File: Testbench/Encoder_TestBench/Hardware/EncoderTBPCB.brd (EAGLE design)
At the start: 51.7 x 81.3 mm, 17 parts, among them IC1 7805DT, U1 ATMEGA328P-PU, X1 C-GRID-05-15-91

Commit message: Upload upon Design Review
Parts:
- removed R3: 1MΩ, resistor:R0603
- C1: value 100nF -> 0.1µF
- C2, C3: value 100nF -> 10µF
- R1: value 220Ω -> 220
- R2: value 200Ω -> 200
- R4: value 850Ω -> 850
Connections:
- net N$10: no longer R3.2
- net N$11: no longer R3.1
- net N$13: now also U1.4; no longer U1.3
- net N$14: now also U1.5; no longer U1.4
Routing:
- net N$14: track 26.9 -> 29.4 mm
- net N$13: track 28.9 -> 31.4 mm
- net N$10: track 39.7 -> 37.8 mm
- net N$11: track 41.4 -> 39.7 mm
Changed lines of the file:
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@@
 </autorouter>
 <elements>
-<element name="C1" library="resistor" package="C0603" value="100nF" x="69.85" y="40.64" rot="R270"/>
-<element name="C2" library="resistor" package="C0603" value="100nF" x="80.01" y="63.5"/>
-<element name="C3" library="resistor" package="C0603" value="100nF" x="83.82" y="63.5"/>
+<element name="C1" library="resistor" package="C0603" value="0.1µF" x="69.85" y="40.64" rot="R270"/>
+<element name="C2" library="resistor" package="C0603" value="10µF" x="80.01" y="63.5"/>
+<element name="C3" library="resistor" package="C0603" value="10µF" x="83.82" y="63.5"/>
 <element name="C4" library="resistor" package="C0603" value="22pF" x="77.47" y="16.51" rot="R180"/>
 <element name="C5" library="resistor" package="C0603" value="22pF" x="85.09" y="16.51"/>
@@
 <element name="JP1" library="pinhead" package="2X03" value="" x="57.15" y="31.75" rot="R90"/>
 <element name="Q1" library="special" package="QS" value="" x="81.28" y="8.89" rot="R180"/>
-<element name="R1" library="resistor" package="R0603" value="220Ω" x="90.17" y="38.1"/>
-<element name="R3" library="resistor" package="R0603" value="1MΩ" x="81.28" y="16.51" rot="R180"/>
-<element name="R4" library="resistor" package="R0603" value="850Ω" x="90.17" y="67.31" rot="R90"/>
+<element name="R1" library="resistor" package="R0603" value="220" x="90.17" y="38.1"/>
+<element name="R4" library="resistor" package="R0603" value="850" x="90.17" y="67.31" rot="R90"/>
 <element name="U1" library="Atmel_By_element14_Batch_1-00" package="DIP254P762X457-28" value="ATMEGA328P-PU" x="74.93" y="57.15" rot="R180">
 <attribute name="OC_FARNELL" value="1715487" x="74.93" y="57.15" size="1.778" layer="27" rot="R180" display="off"/>
@@
 <attribute name="SUPPLIER" value="Atmel" x="74.93" y="57.15" size="1.778" layer="27" rot="R180" display="off"/>
 </element>
-<element name="R2" library="resistor" package="R0603" value="200Ω" x="90.17" y="33.02"/>
+<element name="R2" library="resistor" package="R0603" value="200" x="90.17" y="33.02"/>
 <element name="X1" library="con-molex" package="15-91-05" value="C-GRID-05-15-91" x="53.34" y="13.97" rot="R90"/>
 <element name="JP2" library="pinhead" package="1X16" value="" x="96.52" y="52.07" rot="R270"/>
@@
 </signal>
 <signal name="N$13">
-<contactref element="U1" pad="3"/>
 <contactref element="X1" pad="1"/>
 <wire x1="65.7225" y1="8.89" x2="80.01" y2="23.1775" width="0.254" layer="1"/>
 <wire x1="64.135" y1="8.89" x2="65.7225" y2="8.89" width="0.254" layer="1"/>
-<wire x1="82.55" y1="29.21" x2="80.01" y2="26.67" width="0.254" layer="1"/>
-<wire x1="80.01" y1="26.67" x2="80.01" y2="23.1775" width="0.254" layer="1"/>
+<wire x1="80.01" y1="29.21" x2="80.01" y2="23.1775" width="0.254" layer="1"/>
+<contactref element="U1" pad="4"/>
+<wire x1="80.01" y1="29.21" x2="82.55" y2="31.75" width="0.254" layer="1"/>
 </signal>
 <signal name="N$14">
-<contactref element="U1" pad="4"/>
 <contactref element="X1" pad="3"/>
 <wire x1="66.675" y1="13.97" x2="78.74" y2="26.035" width="0.254" layer="1"/>
 <wire x1="64.135" y1="13.97" x2="66.675" y2="13.97" width="0.254" layer="1"/>
-<wire x1="82.55" y1="31.75" x2="78.74" y2="27.94" width="0.254" layer="1"/>
-<wire x1="78.74" y1="27.94" x2="78.74" y2="26.035" width="0.254" layer="1"/>
+<contactref element="U1" pad="5"/>
+<wire x1="78.74" y1="30.48" x2="82.55" y2="34.29" width="0.254" layer="1"/>
+<wire x1="78.74" y1="26.035" x2="78.74" y2="30.48" width="0.254" layer="1"/>
 </signal>
 <signal name="N$15">
@@
 <contactref element="Q1" pad="2"/>
 <contactref element="C4" pad="1"/>
-<contactref element="R3" pad="2"/>
 <contactref element="U1" pad="9"/>
-<wire x1="80.43" y1="16.51" x2="78.74" y2="16.51" width="0.254" layer="1"/>
 <wire x1="78.74" y1="8.89" x2="78.74" y2="16.51" width="0.254" layer="1"/>
 <wire x1="78.74" y1="16.51" x2="78.32" y2="16.51" width="0.254" layer="1"/>
@@
 <wire x1="80.645" y1="17.145" x2="83.82" y2="20.32" width="0.254" layer="1"/>
 <wire x1="80.645" y1="16.51" x2="80.645" y2="17.145" width="0.254" layer="1"/>
-<wire x1="80.645" y1="16.51" x2="80.43" y2="16.51" width="0.254" layer="1"/>
+<wire x1="78.74" y1="16.51" x2="80.645" y2="16.51" width="0" layer="19" extent="1-1"/>
 </signal>
 <signal name="N$11">
 <contactref element="Q1" pad="1"/>
 <contactref element="C5" pad="1"/>
-<contactref element="R3" pad="1"/>
 <contactref element="U1" pad="10"/>
 <wire x1="83.6676" y1="8.9154" x2="83.82" y2="8.89" width="0.254" layer="16"/>
-<wire x1="83.82" y1="16.51" x2="82.13" y2="16.51" width="0.254" layer="1"/>
 <wire x1="83.82" y1="8.89" x2="83.82" y2="16.51" width="0.254" layer="1"/>
 <wire x1="83.82" y1="16.51" x2="84.24" y2="16.51" width="0.254" layer="1"/>

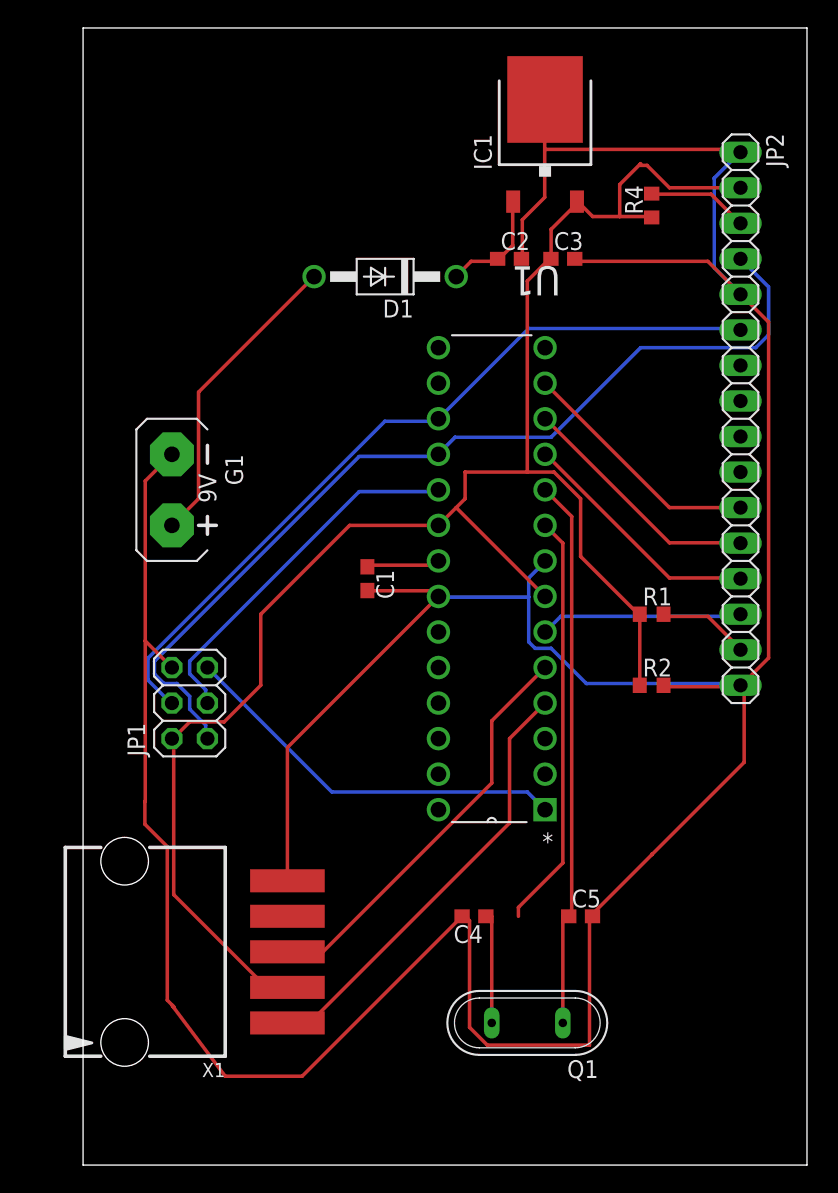
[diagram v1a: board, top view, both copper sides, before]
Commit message: Encoder Post-Review Modification
Board Replaced upon comments given by Daniil and Ryo
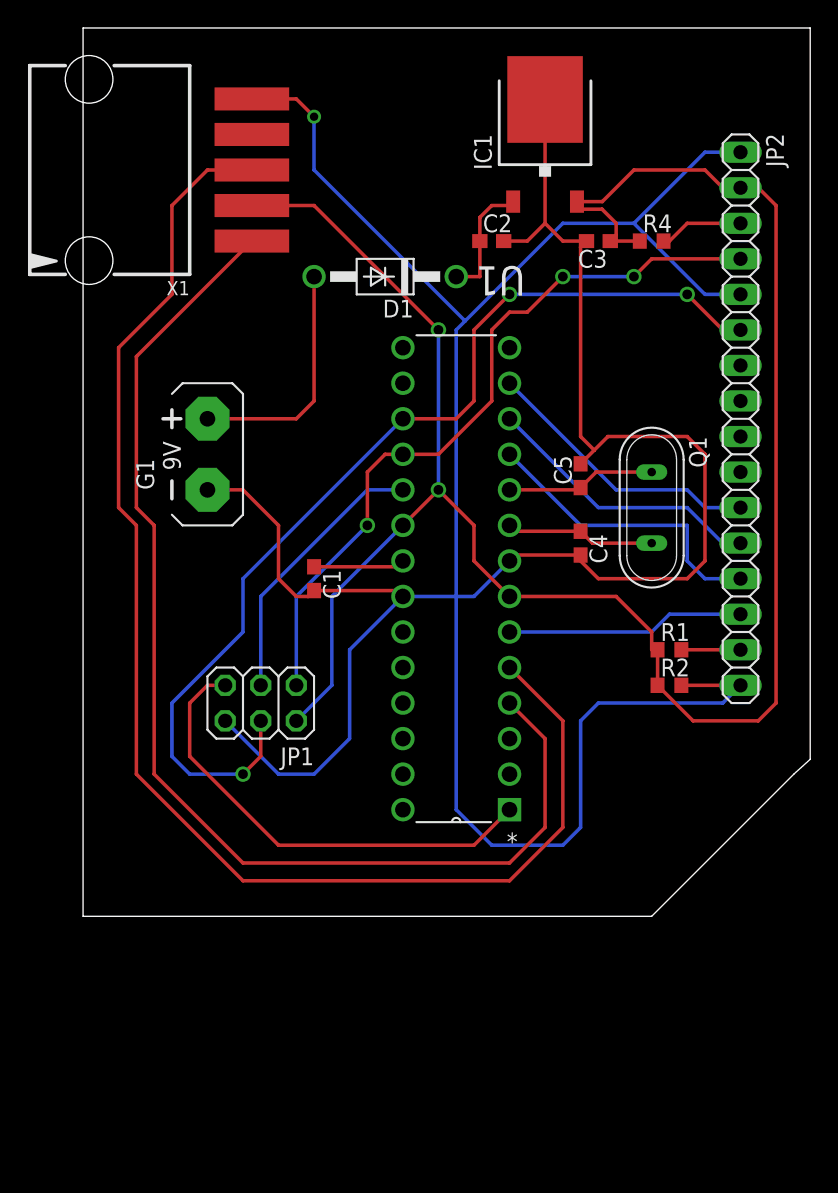
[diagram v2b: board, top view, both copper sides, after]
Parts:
- C2: value 10µF -> 0.33µF
- C3: value 10µF -> 0.1µF
- moved X1 55.9 mm to (50.8, 69.8)
- moved Q1 37.9 mm to (90.2, 45.7), turned to 270 degrees
- moved C5 31.5 mm to (85.1, 48.0), turned to 90 degrees
- moved C4 27.7 mm to (85.1, 43.2), turned to 270 degrees
- moved JP1 5.08 mm to (62.2, 31.8), turned to 180 degrees
- moved C1 3.81 mm to (66.0, 40.6)
- moved G1 3.59 mm to (58.4, 49.5), turned to 0 degrees
- moved C3 2.84 mm to (86.4, 64.8), turned to 180 degrees
- moved R1 2.84 mm to (91.4, 35.6)
- moved R4 2.54 mm to (90.2, 64.8), turned to 0 degrees
- moved U1 2.54 mm to (72.4, 57.1)
- moved C2 1.80 mm to (78.7, 64.8)
- moved R2 1.27 mm to (91.4, 33.0)
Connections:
- net N$1 renamed PB3
- net N$13 renamed ENPA
- net N$14 renamed ENPB
- net N$18 renamed PB5
- net N$19 renamed PC6
- net N$4 renamed P4T14
- net N$5 renamed P5T13
- net N$6 renamed P6T12
- net N$7 renamed P7T11
- net N$9 renamed PB4
- net VSS renamed GND
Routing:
- net ENPB: track 29.4 -> 97.7 mm
- net ENPA: track 31.4 -> 83.6 mm
- net N$11: track 39.7 -> 10.7 mm
- net N$10: track 37.8 -> 10.7 mm
- net GND: track 265.6 -> 244.9 mm, vias 0 -> 1
- net PB3: track 56.1 -> 72.8 mm, vias 0 -> 3
- net VDD: track 127.2 -> 143.5 mm, vias 0 -> 2
- net PB4: track 67.5 -> 53.3 mm, vias 0 -> 3
- net PB5: track 26.4 -> 19.7 mm
- net PC6: track 28.3 -> 33.4 mm
- net N$15: track 22.0 -> 17.0 mm
- net P5T13: track 17.6 -> 21.7 mm
- net P6T12: track 17.6 -> 20.2 mm
- net P7T11: track 17.7 -> 20.2 mm
- net P4T14: track 14.5 -> 17.0 mm
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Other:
- board size 51.7 x 81.3 mm -> 52 x 63.5 mm

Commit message: Testbench Improvement
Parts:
- Q1: value (none) -> 16MHz
- moved R2 66.0 mm to (30.0, 8.89)
- moved C5 64.7 mm to (24.7, 24.9)
- moved C1 63.2 mm to (7.62, 16.5)
- moved C4 63.2 mm to (26.7, 19.1)
- moved D1 63.2 mm to (12.7, 38.1)
- moved G1 63.2 mm to (0.00, 25.4)
- moved Q1 63.2 mm to (31.8, 21.6)
- moved U1 63.2 mm to (14.0, 33.0)
- moved JP1 63.2 mm to (3.81, 7.62)
- moved JP2 63.2 mm to (38.1, 27.9)
- moved X1 63.2 mm to (-7.62, 45.7)
- moved R1 62.3 mm to (34.0, 11.4)
- moved C2 61.9 mm to (21.3, 41.6)
- moved C3 61.9 mm to (28.9, 41.6)
- moved IC1 61.4 mm to (26.1, 48.3)
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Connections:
- net N$10 renamed CRYSTAL
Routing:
- net GND: track 244.9 -> 250.5 mm
- net VDD: track 143.5 -> 146.8 mm
- net VO: track 6.03 -> 3.61 mm
- net N$16: track 8.77 -> 10.3 mm
- net PC6: track 33.4 -> 34.9 mm
- net ENPB: track 97.7 -> 96.6 mm
- net N$2: track 4.23 -> 3.23 mm
- net ENPA: track 83.6 -> 82.8 mm
- net PB3: vias 3 -> 2

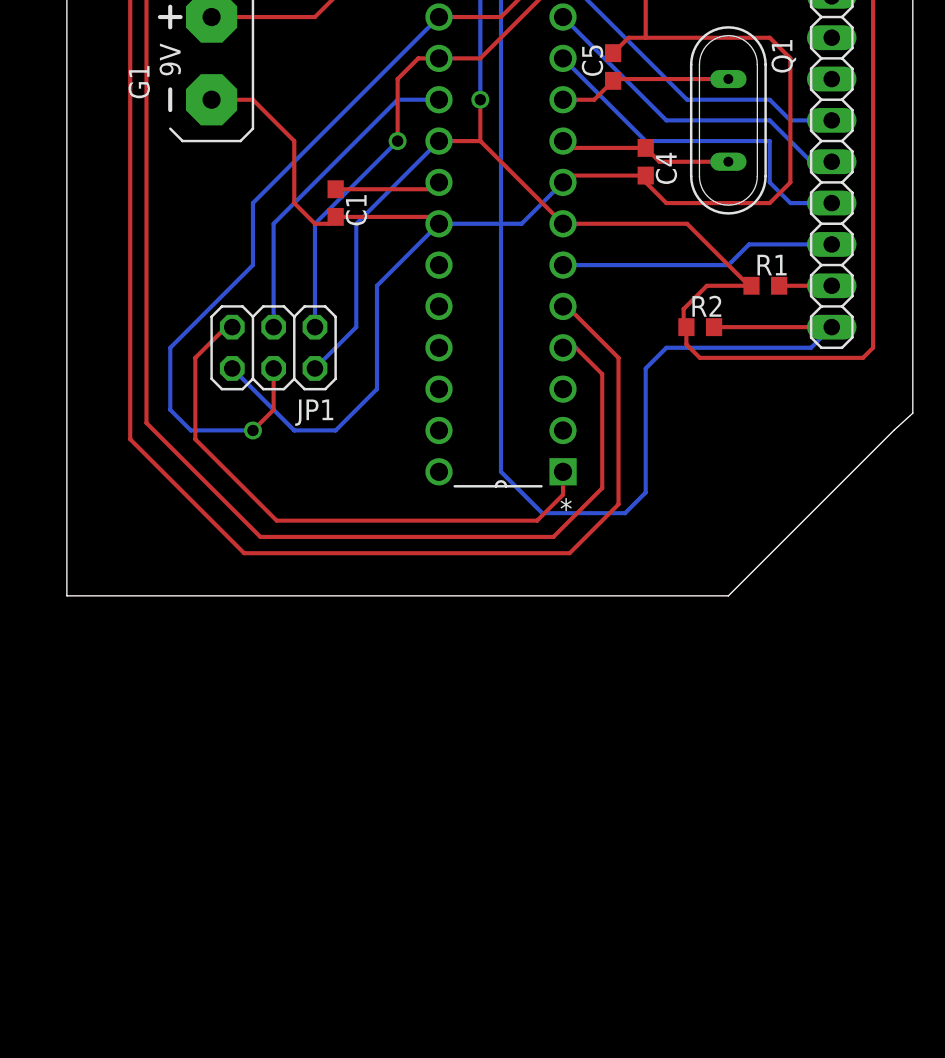
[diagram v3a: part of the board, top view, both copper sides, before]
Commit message: Battery and LCD Overlay
Intended LCD position put as 22 bPlace and Potential Battery put as 21
tPlace on the graph as Graphical reference
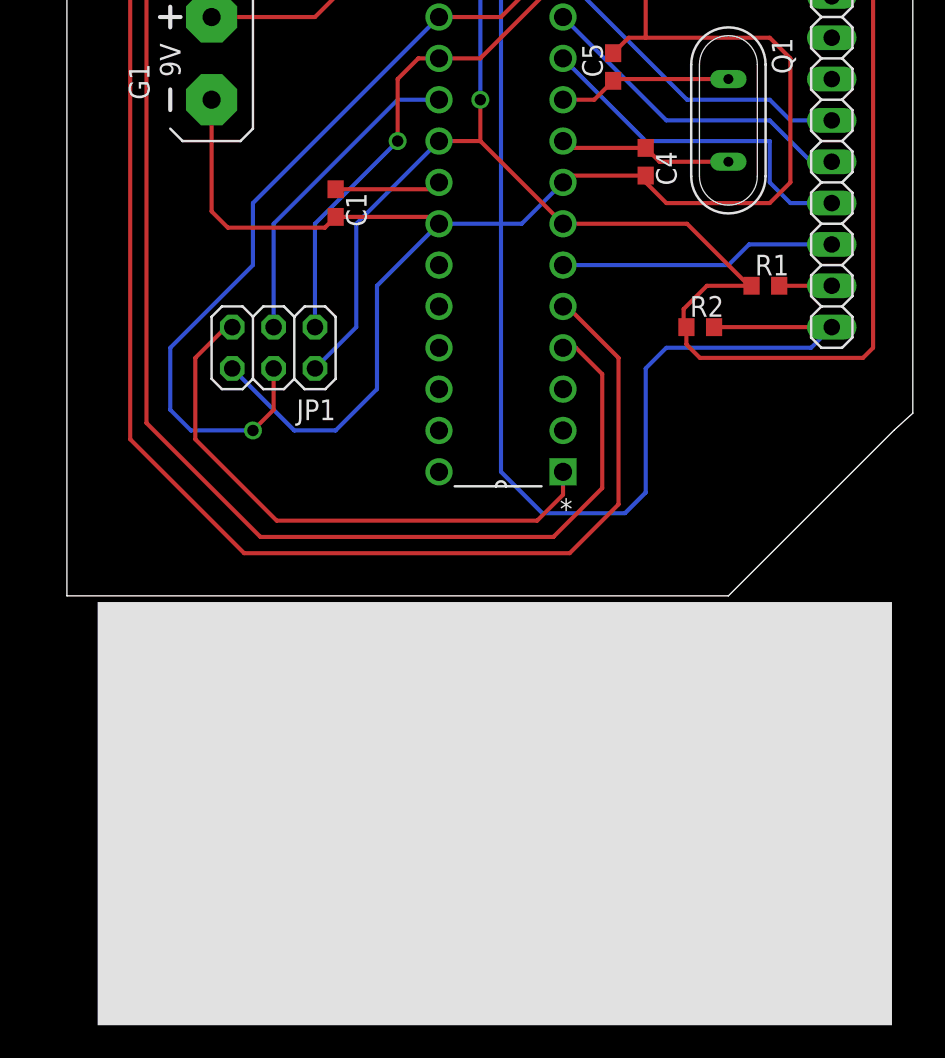
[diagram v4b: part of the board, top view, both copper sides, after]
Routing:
- net GND: track 250.5 -> 252.5 mm
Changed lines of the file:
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@@
 <wire x1="43.08" y1="55.87" x2="-8.89" y2="55.87" width="0" layer="20"/>
 <wire x1="-8.89" y1="55.87" x2="-8.89" y2="-7.62" width="0" layer="20"/>
+<rectangle x1="4.54" y1="-25.5" x2="40.54" y2="54.5" layer="22"/>
+<rectangle x1="-7" y1="-34" x2="41.8" y2="-8" layer="21"/>
 </plain>
 <attributes>
@@
 <wire x1="22.01" y1="18.2" x2="21.59" y2="17.78" width="0.254" layer="1"/>
 <wire x1="13.55" y1="15.66" x2="13.97" y2="15.24" width="0.254" layer="1"/>
-<wire x1="7.2" y1="15.24" x2="7.62" y2="15.66" width="0.254" layer="1"/>
 <wire x1="19.05" y1="15.24" x2="21.59" y2="17.78" width="0.254" layer="16"/>
-<wire x1="0" y1="22.86" x2="2.54" y2="22.86" width="0.254" layer="1"/>
-<wire x1="2.54" y1="22.86" x2="5.08" y2="20.32" width="0.254" layer="1"/>
-<wire x1="5.08" y1="20.32" x2="5.08" y2="16.51" width="0.254" layer="1"/>
-<wire x1="5.08" y1="16.51" x2="6.35" y2="15.24" width="0.254" layer="1"/>
-<wire x1="6.35" y1="15.24" x2="7.2" y2="15.24" width="0.254" layer="1"/>
 <wire x1="26.67" y1="40.22" x2="28.09" y2="41.64" width="0.254" layer="1"/>
 <wire x1="26.67" y1="18.2" x2="26.67" y2="17.78" width="0.254" layer="1"/>
@@
 <wire x1="26.13" y1="50.76" x2="26" y2="51.63" width="0.254" layer="1"/>
 <wire x1="26" y1="51.63" x2="26" y2="41.64" width="0.254" layer="1"/>
+<wire x1="0" y1="22.86" x2="0" y2="16" width="0.254" layer="1"/>
+<wire x1="0" y1="16" x2="1" y2="15" width="0.254" layer="1"/>
+<wire x1="1" y1="15" x2="6.96" y2="15" width="0.254" layer="1"/>
+<wire x1="6.96" y1="15" x2="7.62" y2="15.66" width="0.254" layer="1"/>
 </signal>
 <signal name="P7T11">

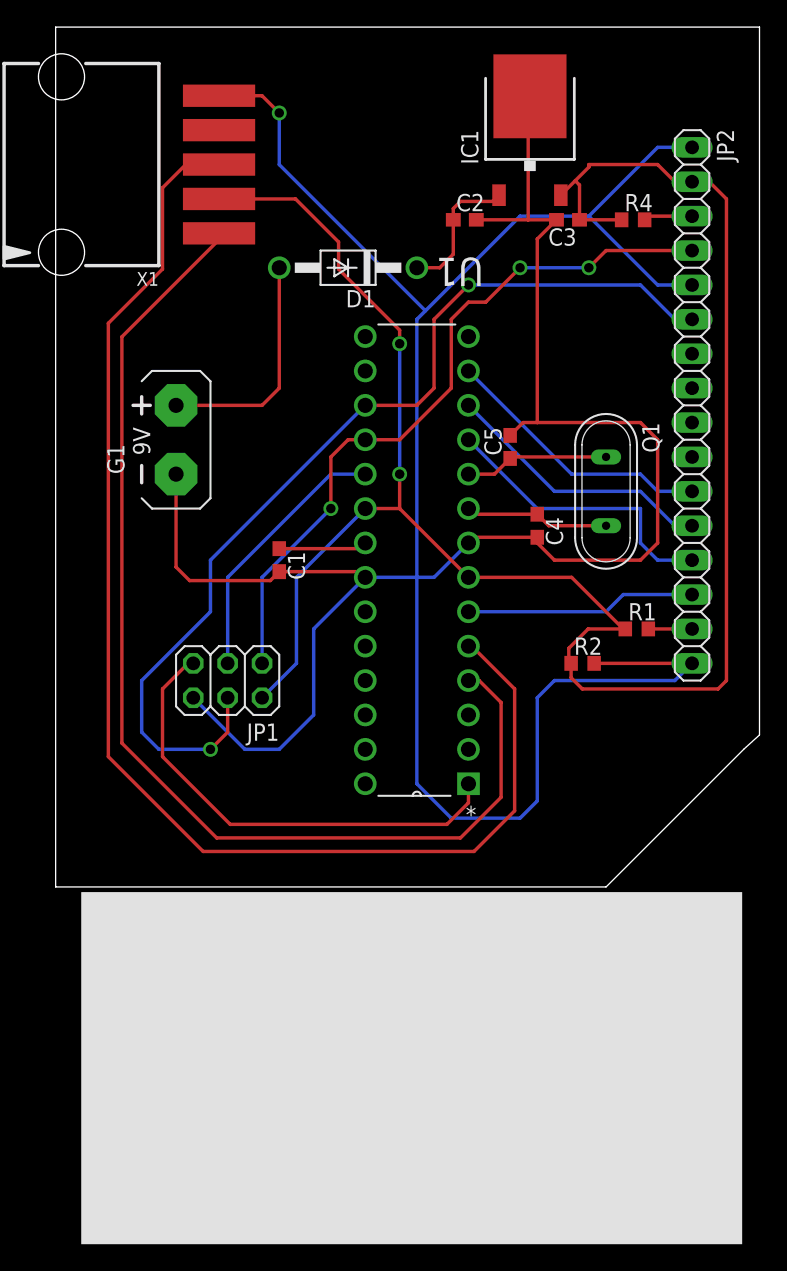
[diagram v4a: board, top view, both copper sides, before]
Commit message: Board Design Updated
Updated w/ ground plane
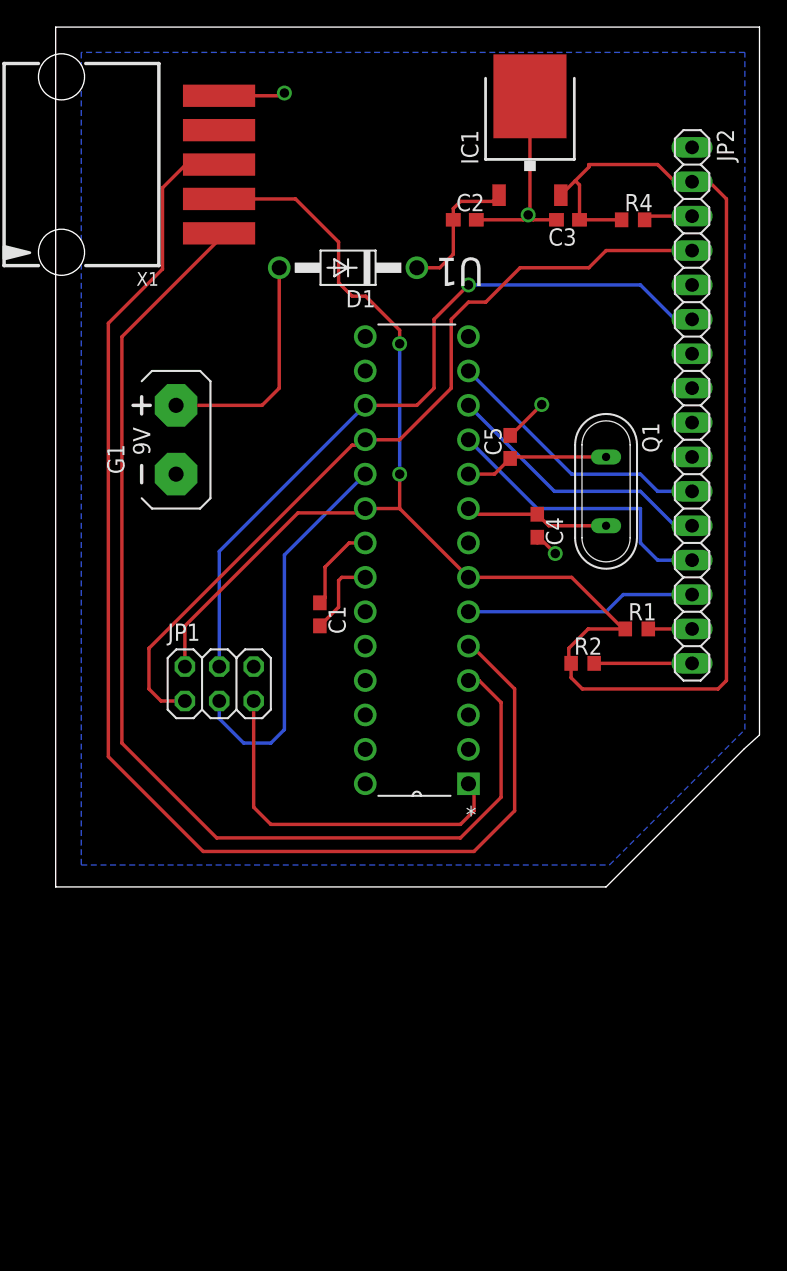
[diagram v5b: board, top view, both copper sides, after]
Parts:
- C1, C3: value 0.1µF -> 0.1uF
- C2: value 0.33µF -> 0.33uF
- moved C1 5.00 mm to (10.6, 12.5)
- moved JP1 0.66 mm to (3.19, 7.38), turned to 0 degrees
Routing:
- net GND: track 252.5 -> 39.7 mm, vias 1 -> 4
- net PB3: track 72.8 -> 55.6 mm, vias 2 -> 1
- net PB5: track 19.7 -> 28.6 mm
- net PB4: track 53.3 -> 61.3 mm, vias 3 -> 0
- net PC6: track 34.9 -> 27.2 mm
- net VDD: track 146.8 -> 150.2 mm
- added copper zone on layer 16, net GND
